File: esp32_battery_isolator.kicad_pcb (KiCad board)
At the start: 4 copper layers, 67.8 x 59.3 mm, 84 parts, among them J1 BATT1, J2 Conn_01x04_Female, J3 USB_B_Micro, J4 BATT2, J5 LOAD1, J6 CHGR, J7 LOAD2, J8 LOAD3, J9 Conn_01x03_Male, Q1 MMBT3904, Q10 AONR21321, Q11 AONR21321, Q12 MMBT3904, Q13 AONR21321, Q2 AONR21321, Q3 MMBT3904, Q4 AONR21321, Q5 MMBT3904, Q6 AONR21321, Q7 MMBT3904, Q8 AONR21321, Q9 MMBT3904, SW1 C492887, SW2 C492887, U1 ESP32-WROOM-32D, U3 ADC128D818, U4 CC6903SO-30A, U5 CH330N, U6 CC6903SO-30A, U7 BL9342

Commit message: REV F - WIP
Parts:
- removed C11: 33p, Capacitor_SMD:C_0603_1608Metric
- removed C13: 100n, Capacitor_SMD:C_0603_1608Metric
- removed C14: 10u, Capacitor_SMD:C_0805_2012Metric
- removed U7: BL9342, Package_TO_SOT_SMD:SOT-23-6
- added C3: 220uF, Capacitor_SMD:C_Elec_6.3x7.7, F.Cu at (112.3, 79.2)
- added D4: LED_Small, LED_SMD:LED_0603_1608Metric, F.Cu at (155.3, 76.8)
- added R25: 11k, Resistor_SMD:R_0603_1608Metric, F.Cu at (137.4, 105.2)
- added R26: 11k, Resistor_SMD:R_0603_1608Metric, F.Cu at (149.4, 118.8)
- added R32: 11k, Resistor_SMD:R_0603_1608Metric, F.Cu at (153.7, 99.5)
- added R33: 11k, Resistor_SMD:R_0603_1608Metric, F.Cu at (167.2, 99.8)
- added R5: 11k, Resistor_SMD:R_0603_1608Metric, F.Cu at (129.8, 88.5)
- added U2: XL1509_SOP8, Package_SO:SOIC-8_3.9x4.9mm_P1.27mm, F.Cu at (119.8, 79.2)
- C2: value 100n -> 10nF
- C8: value 4.7uF -> 220uF; footprint Capacitor_SMD:C_0805_2012Metric -> Capacitor_Tantalum_SMD:CP_EIA-3528-15_AVX-H
- D1: value B5819W -> SS34; footprint Diode_SMD:D_SOD-123 -> Diode_SMD:D_SMA
- L1: value L_Small -> 47uH; footprint Inductor_SMD:L_Taiyo-Yuden_NR-30xx -> Inductor_SMD:L_Bourns_SRN6045TA
- R2: value 124k -> 11k
- R3: value 40.2k -> 3.6k
- moved SW1 37.9 mm to (159.2, 71.8)
- moved SW2 37.3 mm to (168.2, 71.8)
- moved Q12 29.6 mm to (168.2, 96.3)
- moved R9 28.7 mm to (131.7, 118.8), turned to 90 degrees
- moved R3 28.0 mm to (153.6, 76.8), turned to 90 degrees
- moved J9 24.9 mm to (162.9, 97.8), turned to 0 degrees
- moved R8 21.2 mm to (157.2, 76.8), turned to 90 degrees
- moved C8 11.5 mm to (127.2, 79.2), turned to 180 degrees
- moved D1 11.0 mm to (126.8, 73.8), turned to 270 degrees
- moved L1 10.1 mm to (120.2, 72.0)
- moved R2 8.92 mm to (115.5, 74.0)
- moved C9 8.13 mm to (160.8, 93.3), turned to 90 degrees
- moved C2 8.01 mm to (123.7, 78.3), turned to 270 degrees
- moved C10 7.79 mm to (160.8, 89.9), turned to 270 degrees
- moved H1 6.60 mm to (111.2, 72.0)
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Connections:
- C8 pad 1: B2VM -> +3V3
- D1 pad 1: Net-(C13-Pad2) -> +3V3
- L1 pad 1: Net-(C13-Pad2) -> Net-(L1-Pad1)
- Q10 pad 2: LOAD3 -> B2C
- Q10 pad 3: B2C -> LOAD3
- Q11 pad 2: Net-(Q11-Pad2) -> B1C
- Q11 pad 3: B1C -> Net-(Q11-Pad3)
- Q13 pad 2: Net-(Q13-Pad2) -> COM
- Q13 pad 3: COM -> Net-(Q13-Pad3)
- Q2 pad 2: LOAD1 -> B2C
- Q2 pad 3: B2C -> LOAD1
- Q4 pad 2: Net-(Q11-Pad2) -> B1VM
- Q4 pad 3: B1VM -> Net-(Q11-Pad3)
- Q6 pad 2: Net-(Q13-Pad2) -> B2C
- Q6 pad 3: B2C -> Net-(Q13-Pad3)
- Q8 pad 2: LOAD2 -> B2C
- Q8 pad 3: B2C -> LOAD2
- R2 pad 1: Net-(C11-Pad1) -> Net-(R2-Pad1)
- R2 pad 2: +3V3 -> B2VM
- R3 pad 1: Net-(C11-Pad1) -> SYS_LED
- R3 pad 2: GND -> Net-(D4-Pad2)
- R9 pad 1: BOOT -> Net-(Q3-Pad1)
- R9 pad 2: +3V3 -> GND
- U1 pad 37: (no net) -> SYS_LED
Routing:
- net FANON: track 62.2 -> 20.2 mm
- net RPM: track 62.7 -> 20.9 mm, vias 2 -> 0
- net +3V3: track 105.4 -> 146.6 mm, vias 8 -> 7
- net BOOT: track 34.2 -> 63.8 mm, vias 2 -> 1
- net TXD: track 42.9 -> 21.0 mm
- net B2VM: track 207.5 -> 224.5 mm, vias 13 -> 14
- net RXD: track 37.6 -> 21.5 mm
- net B2C: track 12.2 -> 1.60 mm, vias 18 -> 66
- net RST: track 37.0 -> 46.1 mm
- net Net-(L1-Pad1): track 0.00 -> 8.12 mm
- net SYS_LED: track 0.00 -> 8.03 mm
- net GND: track 62.4 -> 69.4 mm, vias 49 -> 68
- net Net-(C11-Pad1): track 5.55 -> 0.00 mm
- net Net-(Q13-Pad1): track 19.9 -> 24.8 mm
- net Net-(R2-Pad1): track 0.00 -> 4.53 mm
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- added copper zone on B.Cu, net GND
- added copper zone on F.Cu, net GND
- added copper zone on B.Cu, net Net-(Q11-Pad3)
- added copper zone on F.Cu, net Net-(Q11-Pad3)
- added copper zone on B.Cu, net Net-(Q13-Pad3)
- added copper zone on F.Cu, net Net-(Q13-Pad3)
- removed copper zone on F.Cu, net +3V3
- removed copper zone on F.Cu, net Net-(C13-Pad2)
- removed copper zone on B.Cu, net Net-(Q11-Pad2)
- removed copper zone on F.Cu, net Net-(Q11-Pad2)
- removed copper zone on B.Cu, net Net-(Q13-Pad2)
- removed copper zone on F.Cu, net Net-(Q13-Pad2)
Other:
- board size 67.8 x 59.3 mm -> 67.8 x 65.8 mm
- rule trace_min: 0.127 -> 0.167
- board text added: "BATTERY ISOLATOR LITE REV. F ACEA QUIGG 08/21"
- board text added: "SYS"
- board text removed: "BATTERY ISOLATOR LITE REV.E ACEA QUIGG 07/21"

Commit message: REV F - off to JLCPCB
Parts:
- removed REF**: KiCad-Logo2_5mm_SilkScreen, Symbol:KiCad-Logo2_5mm_SilkScreen
- Q10, Q11, Q13, Q2, Q4, Q6, Q8: footprint Acea:TRANS_AONR21321 -> Acea:DFN-TRANS_AONR21321
- U5: value CH330N -> CH340N
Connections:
- Q3 pad 3: Net-(Q2-Pad1) -> Net-(Q2-PadG)
- Q5 pad 3: Net-(Q13-Pad1) -> Net-(Q13-PadG)
- Q9 pad 3: Net-(Q10-Pad1) -> Net-(Q10-PadG)
- R15 pad 2: Net-(Q13-Pad1) -> Net-(Q13-PadG)
- R16 pad 2: Net-(Q2-Pad1) -> Net-(Q2-PadG)
- R20 pad 2: Net-(Q10-Pad1) -> Net-(Q10-PadG)
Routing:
- net Net-(Q10-PadG): track 0.00 -> 26.2 mm
- net Net-(Q13-Pad1): track 24.8 -> 0.00 mm
- net Net-(Q10-Pad1): track 23.8 -> 0.00 mm
- net Net-(Q13-PadG): track 0.00 -> 22.5 mm
- net Net-(Q2-Pad1): track 12.3 -> 0.00 mm
- net Net-(Q2-PadG): track 0.00 -> 10.1 mm
- net Net-(Q7-Pad3): track 12.6 -> 10.4 mm
- net Net-(Q7-Pad1): track 6.59 -> 8.19 mm
- net +3V3: track 146.6 -> 145.6 mm
- net Net-(Q11-Pad3): track 0.93 -> 0.00 mm, vias 13 -> 0
- net Net-(Q11-PadD): track 0.00 -> 0.38 mm, vias 0 -> 10
- net LOAD2: track 0.03 -> 0.00 mm, vias 37 -> 30
- net LOAD1: track 0.03 -> 0.00 mm, vias 32 -> 34
- net Net-(Q13-PadD): vias 0 -> 4
- net Net-(Q13-Pad3): vias 8 -> 0
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- added copper zone on B.Cu, net Net-(Q11-PadD)
- added copper zone on F.Cu, net Net-(Q11-PadD)
- added copper zone on B.Cu, net Net-(Q13-PadD)
- added copper zone on F.Cu, net Net-(Q13-PadD)
- removed copper zone on B.Cu, net Net-(Q11-Pad3)
- removed copper zone on F.Cu, net Net-(Q11-Pad3)
- removed copper zone on B.Cu, net Net-(Q13-Pad3)
- removed copper zone on F.Cu, net Net-(Q13-Pad3)

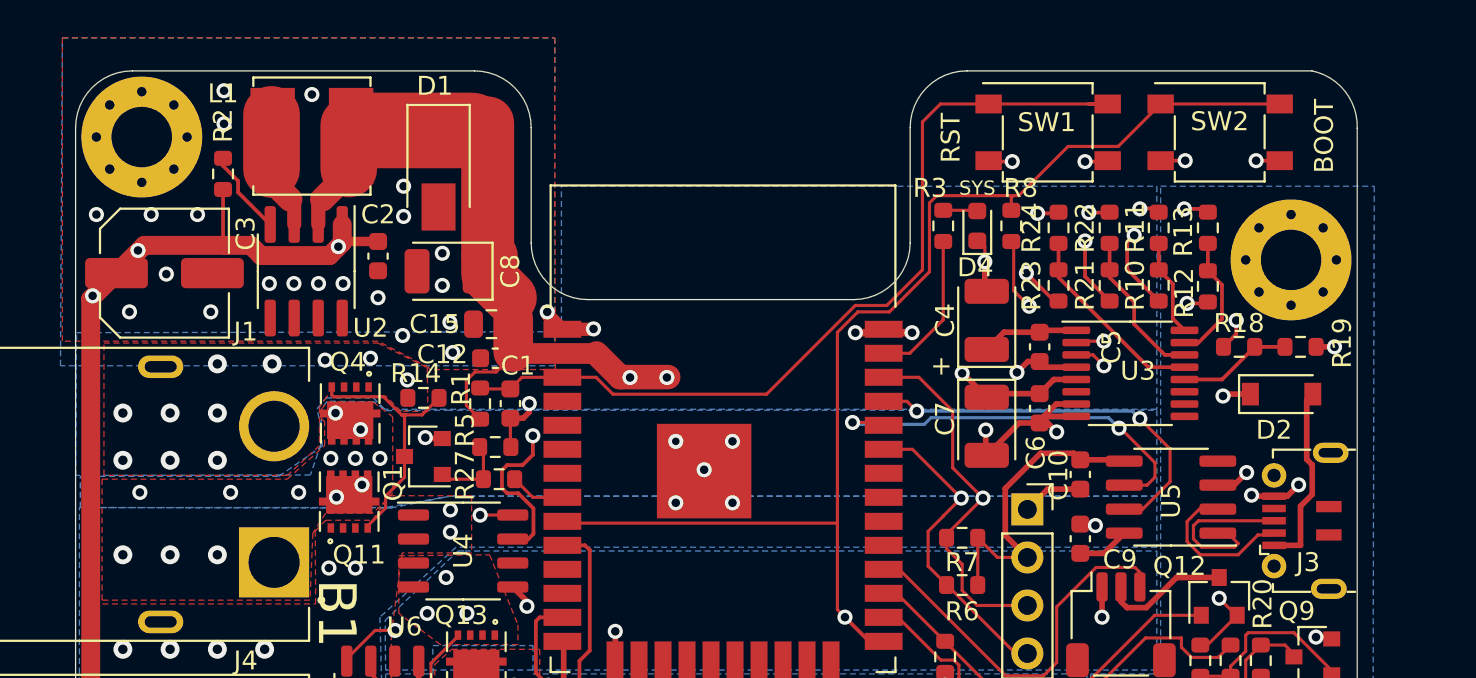
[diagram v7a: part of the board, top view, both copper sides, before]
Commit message: Getting closer to finished
Big changes to the app to make it simpler
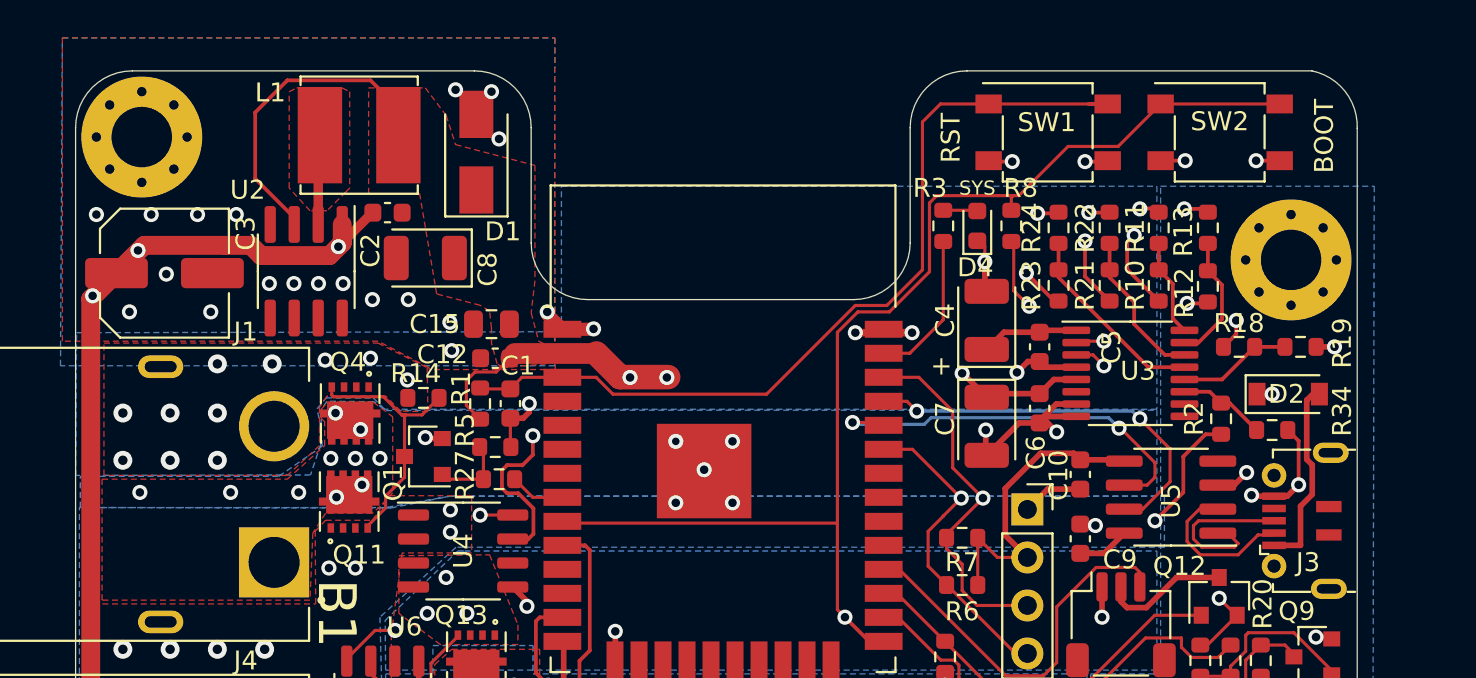
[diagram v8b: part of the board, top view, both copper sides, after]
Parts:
- added R34: 33k, Resistor_SMD:R_0603_1608Metric, F.Cu at (170.9, 87.5)
- C2: value 10nF -> 1uF
- R2: value 11k -> 200k
- moved R2 54.4 mm to (168.2, 87.0), turned to 90 degrees
- moved L1 2.50 mm to (122.7, 72.0)
- moved C2 2.35 mm to (124.2, 76.0), turned to 0 degrees
- moved D1 2.19 mm to (128.8, 72.8), turned to 90 degrees
- moved C8 1.30 mm to (126.2, 78.5)
- moved D2 0.35 mm to (171.8, 85.7)
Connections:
- R2 pad 1: Net-(R2-Pad1) -> B1C
- R2 pad 2: B2VM -> B1CD
- U2 pad 2: +3V3 -> Net-(L1-Pad1)
- U2 pad 3: Net-(L1-Pad1) -> +3V3
- U2 pad 4: Net-(R2-Pad1) -> (no net)
- U3 pad 11: (no net) -> B1CD
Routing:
- net +3V3: track 145.6 -> 138.2 mm
- net B1C: track 0.00 -> 6.51 mm, vias 49 -> 50
- net B1CD: track 0.00 -> 4.65 mm
- net Net-(R2-Pad1): track 4.53 -> 0.00 mm
- net Net-(L1-Pad1): track 8.12 -> 4.76 mm
- net GND: track 69.4 -> 72.5 mm, vias 64 -> 61
- net (no net): vias 3 -> 0
- added copper zone on F.Cu, net +3V3
- added copper zone on F.Cu, net Net-(L1-Pad1)
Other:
- board text added: "BATTERY ISOLATOR LITE REV. G ACEA QUIGG 09/21"
- board text removed: "BATTERY ISOLATOR LITE REV. F ACEA QUIGG 08/21"
